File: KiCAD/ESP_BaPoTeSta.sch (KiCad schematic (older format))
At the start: 35 parts, among them P1 ProgHdr, P10 CONN_01X04, P13 CONN_01X03, P15 CONN_01X04, P2 Battery, P3 MicroUSB, P4 Flash, P5 Conf, P9 CONN_01X04, Q1 IRLML6302, U1 MCP1700-330, U2 ESP-12, U3 MCP73831-2-OT

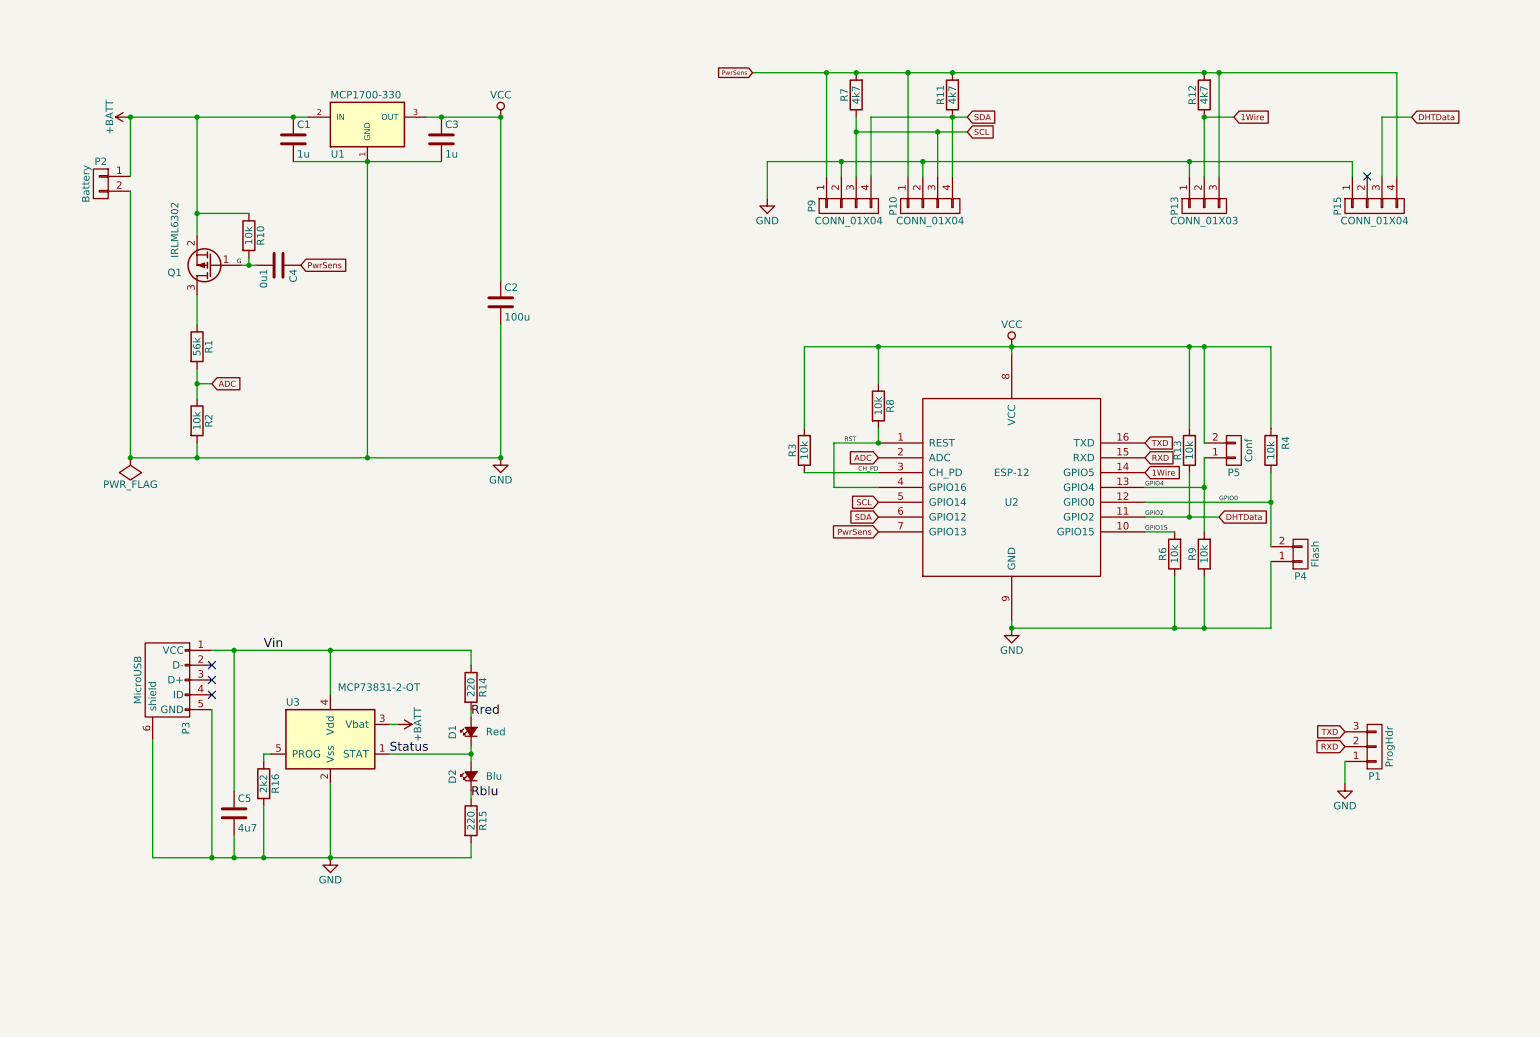
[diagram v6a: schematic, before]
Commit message: ENH: PCB: Prevent undervoltage
If the undervoltage-sensor NCP300 senses too low a battery voltage,
it will tie its output to GND, thus switching off the BSS806N
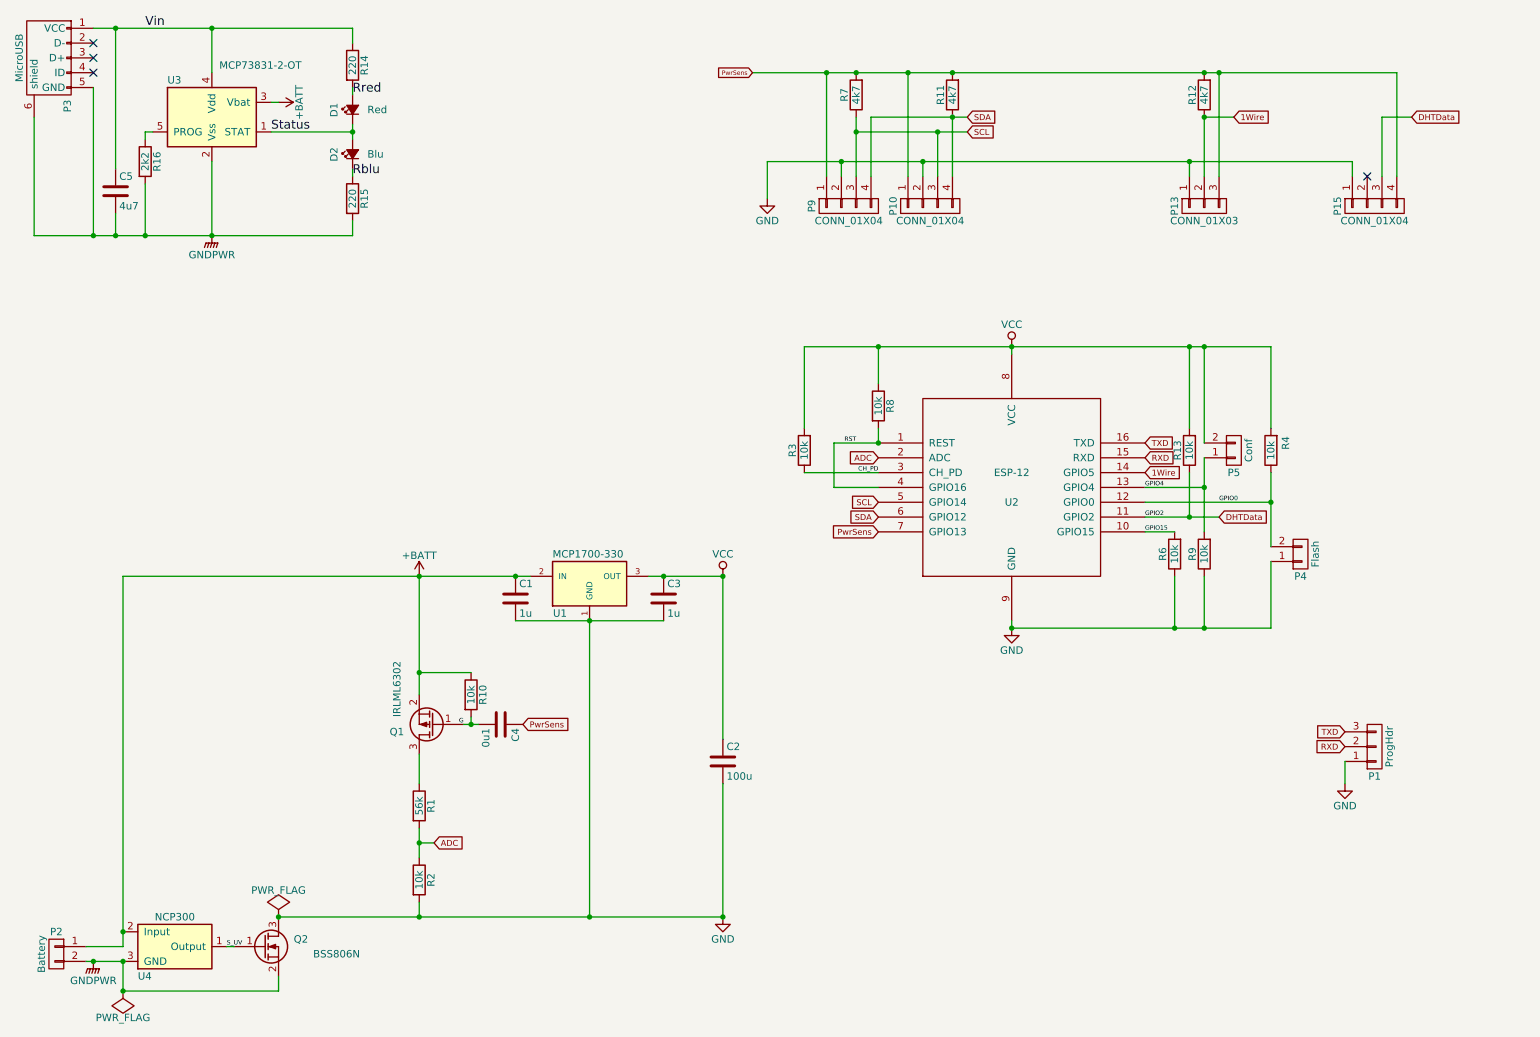
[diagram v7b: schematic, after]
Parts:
- added Q2: BSS806N, TO_SOT_Packages_SMD:SOT-23_Handsoldering, symbol Q_NMOS_GSD
- added U4: NCP300, TO_SOT_Packages_SMD:SOT-23-5, symbol NCP300
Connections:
- net +BATT: now also U4.2 (Input)
- net GND: now also Q2.3 (D); no longer C5.2, P2.2 (P2), P3.5 (GND), P3.6 (shield), R15.2, R16.2, U3.2 (Vss)
- new net GNDPWR: C5.2, P2.2 (P2), P3.5 (GND), P3.6 (shield), Q2.2 (S), R15.2, R16.2, U3.2 (Vss), U4.3 (GND)
- new net S_UV: Q2.1 (G), U4.1 (Output)
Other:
- moved on the sheet: C1, C2, C3, C4, C5, D1, D2, P2, P3, Q1, R1, R10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

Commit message: DOC: SCH: Improve schematic layout
Join battery charger and voltage regulation parts
Move parts around
Fix Rev/Date
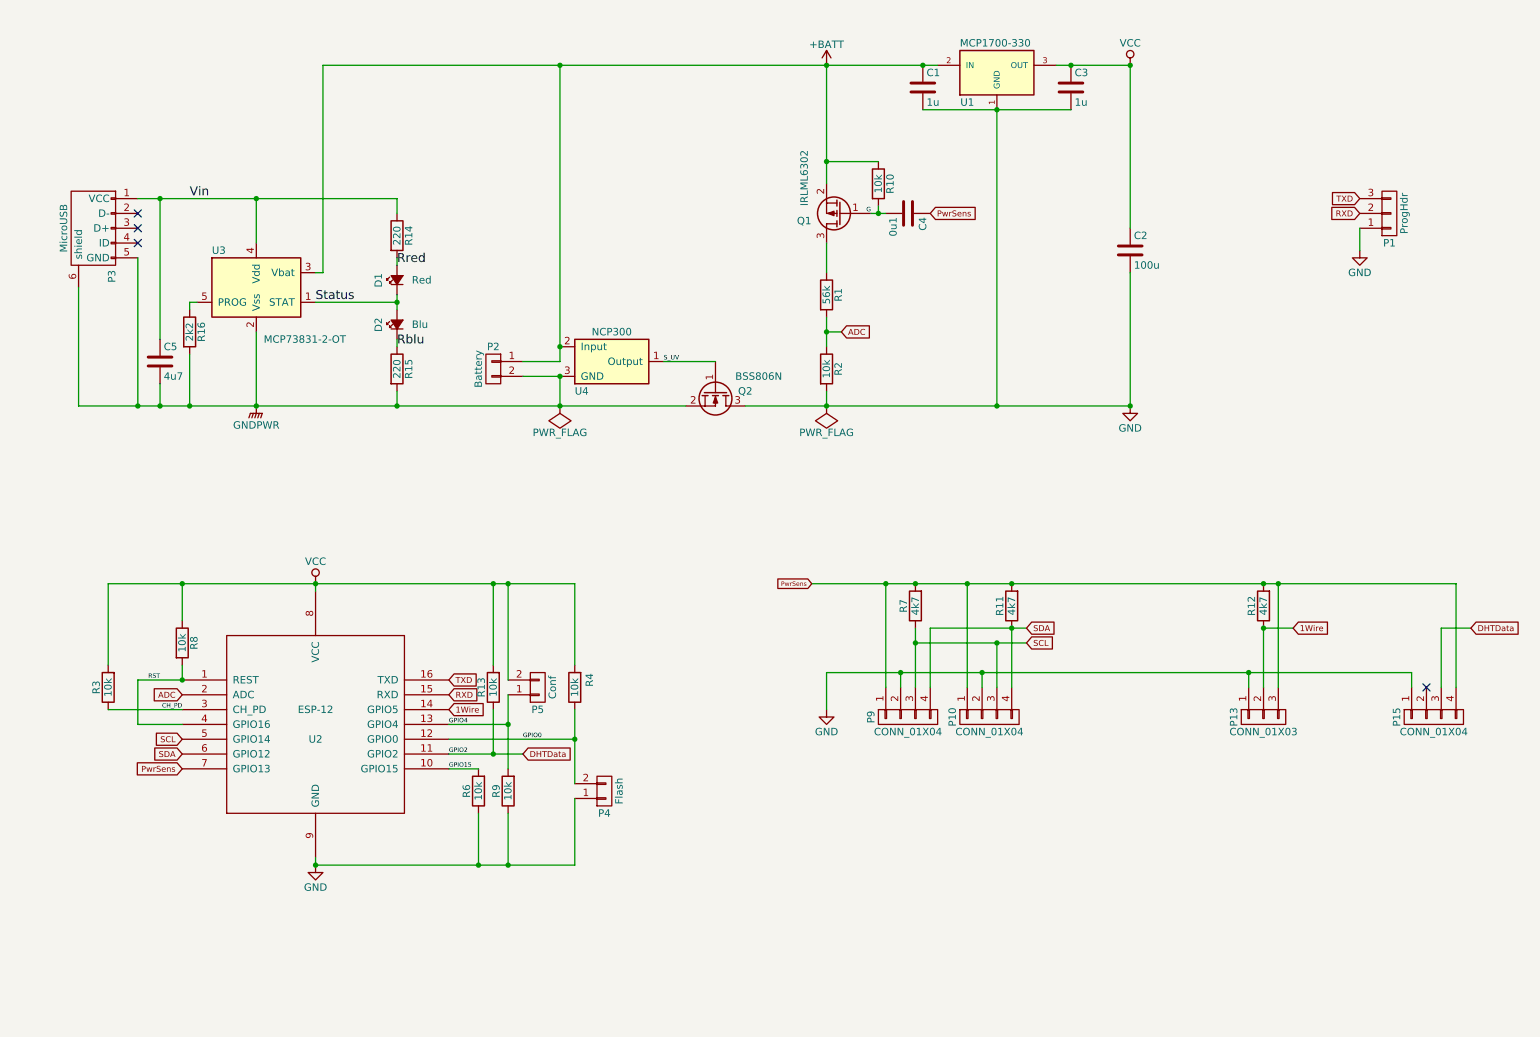
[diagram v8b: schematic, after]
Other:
- moved on the sheet: C1, C2, C3, C4, C5, D1, D2, P1, P10, P13, P15, P2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
